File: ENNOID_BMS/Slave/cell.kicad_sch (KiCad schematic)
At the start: 6 parts, among them Q16 TSM2323

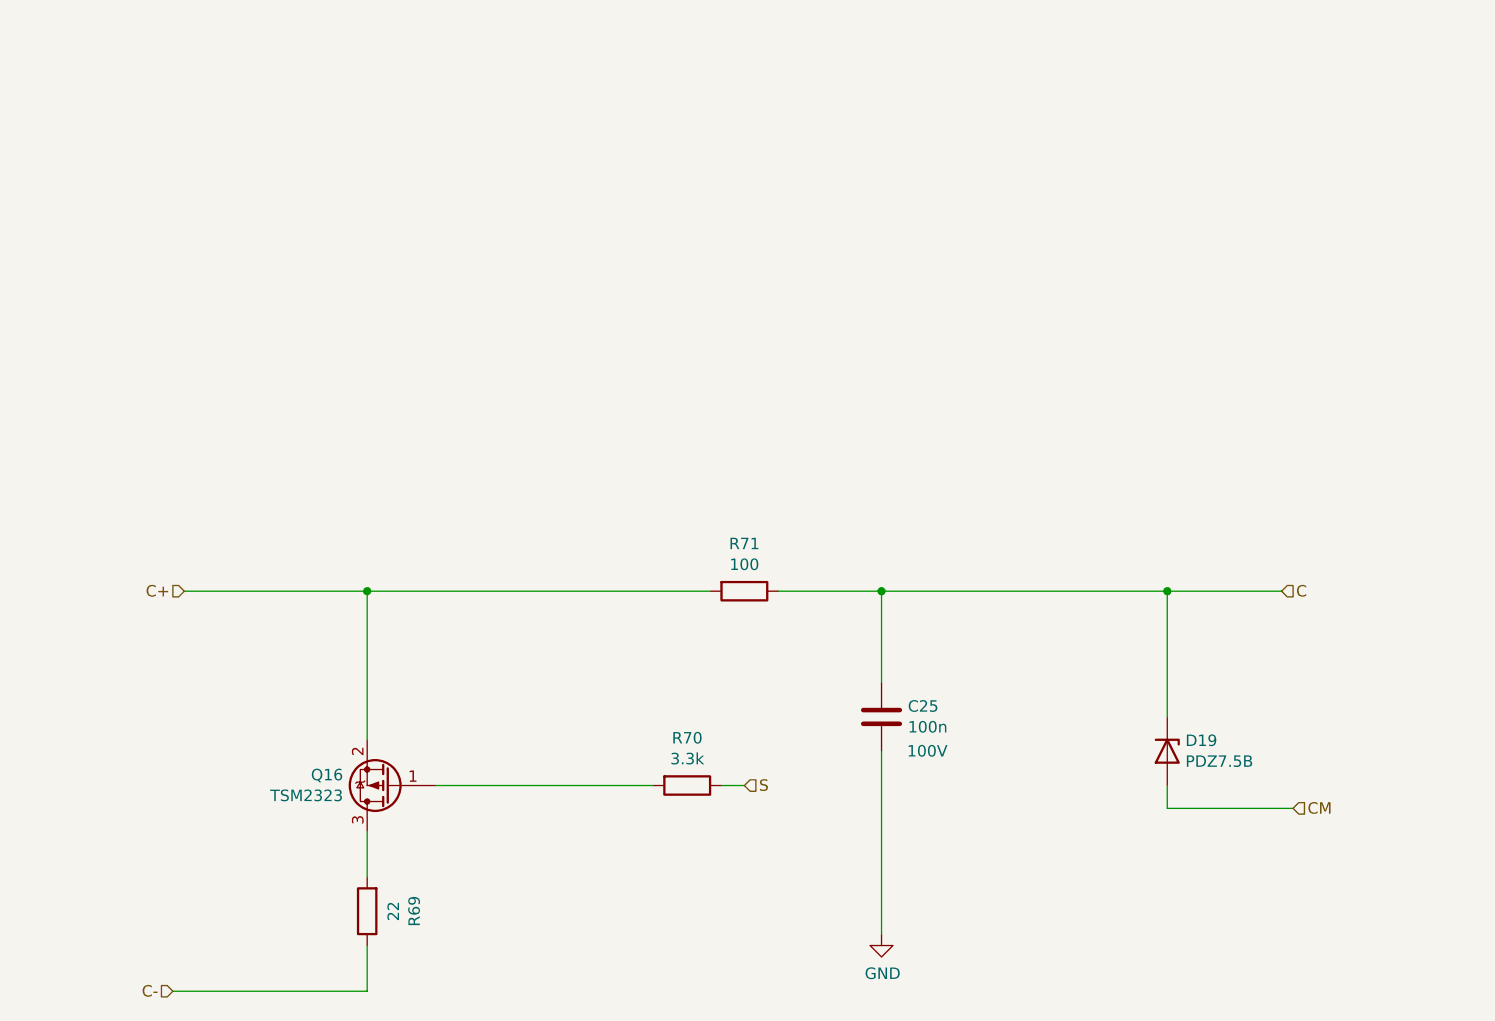
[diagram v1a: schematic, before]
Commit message: fused slave variant v1
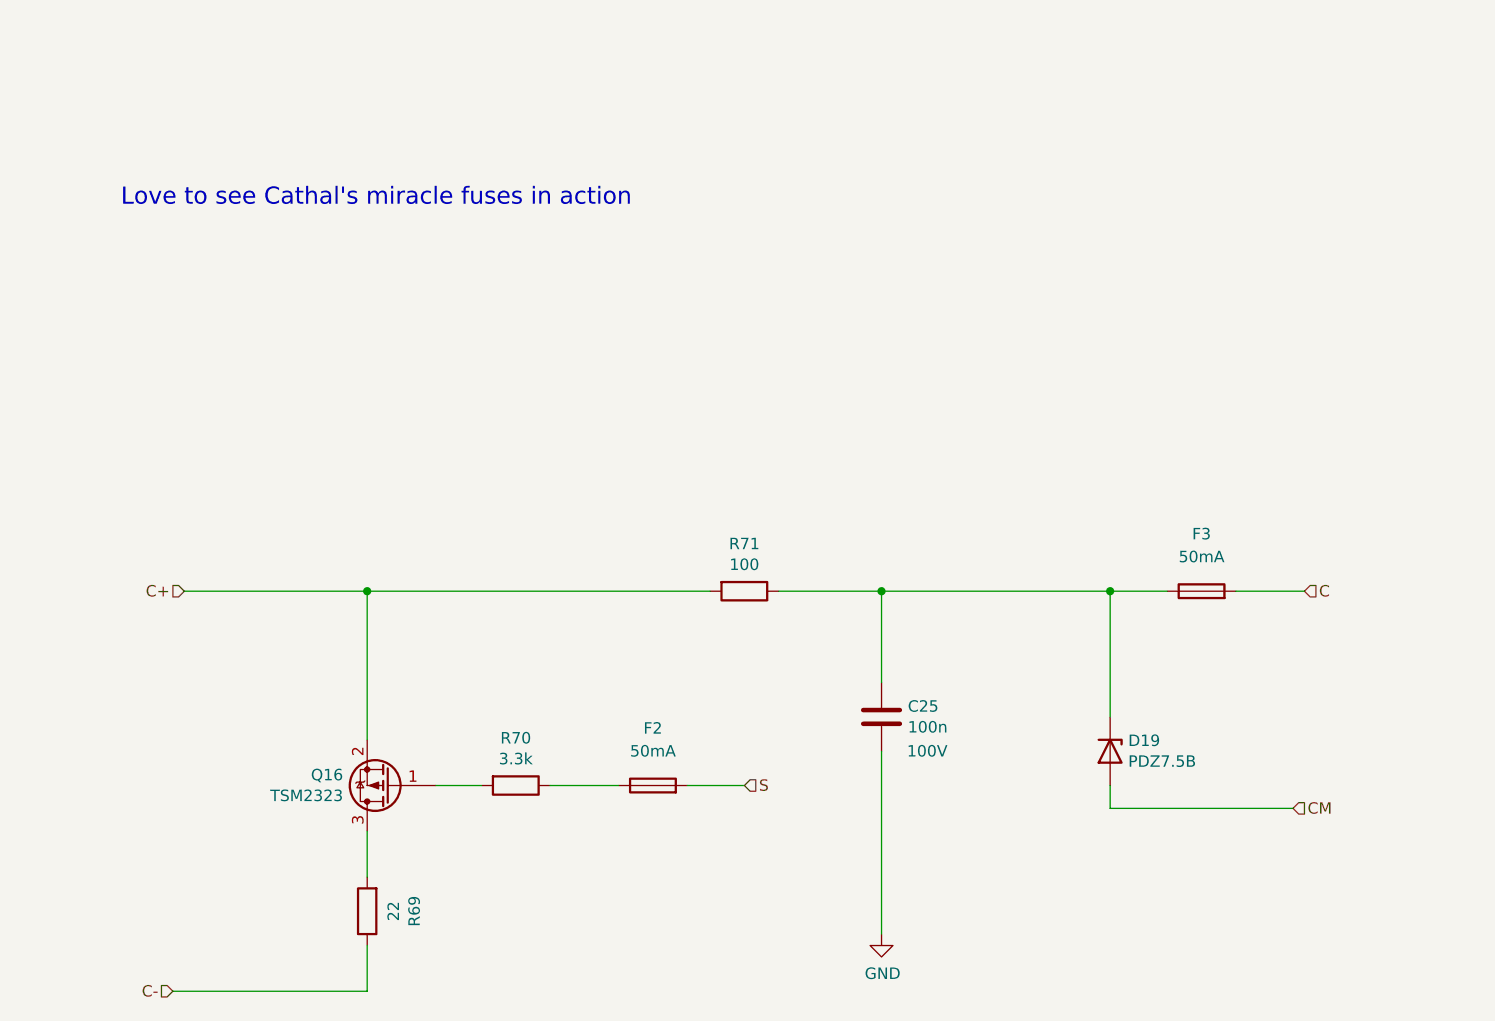
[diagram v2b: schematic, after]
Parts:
- added F2, F3: 50mA, Fuse:Fuse_0603_1608Metric, symbol Device:Fuse
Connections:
- net C: now also F3.2; no longer C25.2, D19.1 (K), R71.1
- net S: now also F2.2; no longer R70.1
- new net: C25.2, D19.1 (K), F3.1, R71.1
- new net: F2.1, R70.1
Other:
- note added: "Love to see Cathal's miracle fuses in action"
- moved on the sheet: D19, R70

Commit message: fuse boards
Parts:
- removed F2: 50mA, Fuse:Fuse_0603_1608Metric, symbol Device:Fuse
- Q16: Part Number TSM2323 -> TSM2323CX RFG
- R70: footprint Resistor_SMD:R_0603_1608Metric -> Resistor_SMD:R_0508_1220Metric; Part Number CRCW06033K30FKEA -> WK73R2ATTD3301F
- R71: Part Number CRCW0603100RFKEA -> RCS0603100RFKEA
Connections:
- net S: now also R70.1
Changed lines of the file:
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@@
 	(wire
 		(pts
-			(xy 106.68 104.14) (xy 114.3 104.14)
+			(xy 106.68 104.14) (xy 116.84 104.14)
 		)
 		(stroke
@@
 		(pts
 			(xy 66.04 82.55) (xy 86.36 82.55)
-		)
-		(stroke
-			(width 0)
-			(type default)
-		)
-	)
-	(wire
-		(pts
-			(xy 121.92 104.14) (xy 128.27 104.14)
 		)
 		(stroke
@@
 	(hierarchical_label "S"
 		(shape input)
-		(at 128.27 104.14 0)
+		(at 116.84 104.14 0)
 		(effects
 			(font
@@
 			)
 		)
-		(property "Datasheet" "https://www.vishay.com/docs/20043/crcwhpe3.pdf"
+		(property "Datasheet" "https://www.vishay.com/doc?20065"
 			(at 128.27 82.55 0)
 			(effects
@@
 			)
 		)
-		(property "Part Number" "CRCW0603100RFKEA"
+		(property "Part Number" "RCS0603100RFKEA"
 			(at 128.27 82.55 90)
 			(effects
@@
 			)
 		)
-		(property "Footprint" "Resistor_SMD:R_0603_1608Metric"
+		(property "Footprint" "Resistor_SMD:R_0508_1220Metric"
 			(at 102.87 102.362 90)
 			(effects
@@
 			)
 		)
-		(property "Datasheet" "https://www.vishay.com/docs/20035/dcrcwe3.pdf"
+		(property "Datasheet" "https://www.koaspeer.com/pdfs/WK73R.pdf"
 			(at 102.87 104.14 0)
 			(effects
@@
 			)
 		)
-		(property "Part Number" "CRCW06033K30FKEA"
+		(property "Part Number" "WK73R2ATTD3301F"
 			(at 102.87 104.14 90)
 			(effects
@@
 			)
 		)
-		(property "Part Number" "TSM2323"
+		(property "Part Number" "TSM2323CX RFG"
 			(at 88.9 104.14 0)
 			(effects
@@
 					(unit 1)
 				)
-			)
-		)
-	)
-	(symbol
-		(lib_id "Device:Fuse")
-		(at 118.11 104.14 90)
-		(unit 1)
-		(exclude_from_sim no)
-		(in_bom yes)
-		(on_board yes)
-		(dnp no)
-		(fields_autoplaced yes)
-		(property "Reference" "F2"
-			(at 118.11 97.79 90)
-			(effects
-				(font
-					(size 1.27 1.27)
-				)
-			)
-		)
-		(property "Value" "50mA"
-			(at 118.11 100.33 90)
-			(effects
-				(font
-					(size 1.27 1.27)
-				)
-			)
-		)
-		(property "Footprint" "Fuse:Fuse_0603_1608Metric"
-			(at 118.11 105.918 90)
-			(effects
-				(font
-					(size 1.27 1.27)
-				)
-				(hide yes)
-			)
-		)
-		(property "Datasheet" "https://www.farnell.com/datasheets/4426720.pdf"
-			(at 118.11 104.14 0)
-			(effects
-				(font
-					(size 1.27 1.27)
-				)
-				(hide yes)
-			)
-		)
-		(property "Description" "Fuse"
-			(at 118.11 104.14 0)
-			(effects
-				(font
-					(size 1.27 1.27)
-				)
-				(hide yes)
-			)
-		)
-		(property "Part Number" "F0603G0R05FNTR"
-			(at 118.11 104.14 90)
-			(effects
-				(font
-					(size 1.27 1.27)
-				)
-				(hide yes)
-			)
-		)
-		(pin "1"
-		)
-		(pin "2"
-		)
-		(instances
-			(project "LTC6812-15W"
-				(path "/2d3f1ad3-25f4-49ef-8b25-1989df14b0f9/00000000-0000-0000-0000-00005b4fcc47"
-					(reference "F33")
-					(unit 1)
-				)
-				(path "/2d3f1ad3-25f4-49ef-8b25-1989df14b0f9/00000000-0000-0000-0000-00005b4fd503"
-					(reference "F31")
-					(unit 1)
-				)
-				(path "/2d3f1ad3-25f4-49ef-8b25-1989df14b0f9/00000000-0000-0000-0000-00005b50012a"
-					(reference "F29")
-					(unit 1)
-				)
-				(path "/2d3f1ad3-25f4-49ef-8b25-1989df14b0f9/00000000-0000-0000-0000-00005b502fef"
-					(reference "F27")
-					(unit 1)
-				)
-				(path "/2d3f1ad3-25f4-49ef-8b25-1989df14b0f9/00000000-0000-0000-0000-00005b50355c"
-					(reference "F25")
-					(unit 1)
-				)
-				(path "/2d3f1ad3-25f4-49ef-8b25-1989df14b0f9/00000000-0000-0000-0000-00005b504105"
-					(reference "F23")
-					(unit 1)
-				)
-				(path "/2d3f1ad3-25f4-49ef-8b25-1989df14b0f9/00000000-0000-0000-0000-00005b504814"
-					(reference "F21")
-					(unit 1)
-				)
-				(path "/2d3f1ad3-25f4-49ef-8b25-1989df14b0f9/00000000-0000-0000-0000-00005b5050bc"
-					(reference "F16")
-					(unit 1)
-				)
-				(path "/2d3f1ad3-25f4-49ef-8b25-1989df14b0f9/00000000-0000-0000-0000-00005b50594b"
-					(reference "F14")
-					(unit 1)
-				)
-				(path "/2d3f1ad3-25f4-49ef-8b25-1989df14b0f9/00000000-0000-0000-0000-00005b506bb1"
-					(reference "F12")
-					(unit 1)
-				)
-				(path "/2d3f1ad3-25f4-49ef-8b25-1989df14b0f9/00000000-0000-0000-0000-00005b507536"
-					(reference "F10")
-					(unit 1)
-				)
-				(path "/2d3f1ad3-25f4-49ef-8b25-1989df14b0f9/00000000-0000-0000-0000-00005b50804f"
-					(reference "F8")
-					(unit 1)
-				)
-				(path "/2d3f1ad3-25f4-49ef-8b25-1989df14b0f9/00000000-0000-0000-0000-00005b508c6c"
-					(reference "F6")
-					(unit 1)
-				)
-				(path "/2d3f1ad3-25f4-49ef-8b25-1989df14b0f9/00000000-0000-0000-0000-00005b509a8b"
-					(reference "F4")
-					(unit 1)
-				)
-				(path "/2d3f1ad3-25f4-49ef-8b25-1989df14b0f9/00000000-0000-0000-0000-00005b50aaba"
-					(reference "F2")
-					(unit 1)
-				)
-			)
-			(project ""
-				(path "/952f467e-ad2b-47b9-b7a8-afd1294da234"
-					(reference "F1")
-					(unit 1)
-				)

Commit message: master and slave updated
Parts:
- F3: footprint Fuse:Fuse_0603_1608Metric -> Fuse:Fuse_1206_3216Metric; Part Number F0603G0R05FNTR -> 3413.0002.11
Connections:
- net C: now also C25.2, D19.1 (K)
- net at F3.1, R71.1: no longer C25.2, D19.1 (K)
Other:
- moved on the sheet: C25, D19, F3, R71
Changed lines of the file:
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@@
 	(text "Love to see Cathal's miracle fuses in action"
 		(exclude_from_sim no)
-		(at 87.376 38.862 0)
+		(at 88.9 21.082 0)
 		(effects
 			(font
@@
 			)
 		)
-	)
-	(junction
-		(at 168.91 82.55)
-		(diameter 0)
-		(color 0 0 0 0)
 	)
 	(junction
@@
 	)
 	(junction
-		(at 143.51 82.55)
+		(at 158.75 82.55)
 		(diameter 0)
 		(color 0 0 0 0)
 	)
-	(wire
-		(pts
-			(xy 168.91 96.52) (xy 168.91 82.55)
-		)
-		(stroke
-			(width 0)
-			(type default)
-		)
-	)
-	(wire
-		(pts
-			(xy 143.51 82.55) (xy 143.51 92.71)
+	(junction
+		(at 184.15 82.55)
+		(diameter 0)
+		(color 0 0 0 0)
+	)
+	(wire
+		(pts
+			(xy 148.59 82.55) (xy 158.75 82.55)
+		)
+		(stroke
+			(width 0)
+			(type default)
+		)
+	)
+	(wire
+		(pts
+			(xy 184.15 96.52) (xy 184.15 82.55)
+		)
+		(stroke
+			(width 0)
+			(type default)
+		)
+	)
+	(wire
+		(pts
+			(xy 158.75 82.55) (xy 158.75 92.71)
 		)
 		(stroke
@@
 	(wire
 		(pts
-			(xy 168.91 106.68) (xy 189.23 106.68)
-		)
-		(stroke
-			(width 0)
-			(type default)
-		)
-	)
-	(wire
-		(pts
-			(xy 86.36 82.55) (xy 124.46 82.55)
+			(xy 184.15 106.68) (xy 204.47 106.68)
+		)
+		(stroke
+			(width 0)
+			(type default)
+		)
+	)
+	(wire
+		(pts
+			(xy 184.15 82.55) (xy 205.74 82.55)
+		)
+		(stroke
+			(width 0)
+			(type default)
+		)
+	)
+	(wire
+		(pts
+			(xy 86.36 82.55) (xy 110.49 82.55)
 		)
 		(stroke
@@
 	(wire
 		(pts
-			(xy 143.51 100.33) (xy 143.51 120.65)
+			(xy 118.11 82.55) (xy 140.97 82.55)
+		)
+		(stroke
+			(width 0)
+			(type default)
+		)
+	)
+	(wire
+		(pts
+			(xy 158.75 100.33) (xy 158.75 120.65)
 		)
 		(stroke
@@
 	(wire
 		(pts
-			(xy 168.91 104.14) (xy 168.91 106.68)
+			(xy 184.15 104.14) (xy 184.15 106.68)
 		)
 		(stroke
@@
 	(wire
 		(pts
-			(xy 143.51 82.55) (xy 168.91 82.55)
-		)
-		(stroke
-			(width 0)
-			(type default)
-		)
-	)
-	(wire
-		(pts
-			(xy 132.08 82.55) (xy 143.51 82.55)
-		)
-		(stroke
-			(width 0)
-			(type default)
-		)
-	)
-	(wire
-		(pts
-			(xy 182.88 82.55) (xy 190.5 82.55)
+			(xy 158.75 82.55) (xy 184.15 82.55)
 		)
 		(stroke
@@
 		(pts
 			(xy 93.98 104.14) (xy 99.06 104.14)
-		)
-		(stroke
-			(width 0)
-			(type default)
-		)
-	)
-	(wire
-		(pts
-			(xy 168.91 82.55) (xy 175.26 82.55)
 		)
 		(stroke
@@
 	(hierarchical_label "C"
 		(shape input)
-		(at 190.5 82.55 0)
+		(at 205.74 82.55 0)
 		(effects
 			(font
@@
 	(hierarchical_label "CM"
 		(shape input)
-		(at 189.23 106.68 0)
+		(at 204.47 106.68 0)
 		(effects
 			(font
@@
 	(symbol
 		(lib_id "Device:R")
-		(at 128.27 82.55 270)
+		(at 114.3 82.55 270)
 		(unit 1)
 		(exclude_from_sim no)
@@
 		(dnp no)
 		(property "Reference" "R71"
-			(at 128.27 77.2922 90)
+			(at 114.3 77.2922 90)
 			(effects
 				(font
@@
 		)
 		(property "Value" "100"
-			(at 128.27 79.6036 90)
+			(at 114.3 79.6036 90)
 			(effects
 				(font
@@
 		)
 		(property "Footprint" "Resistor_SMD:R_0603_1608Metric"
-			(at 128.27 80.772 90)
+			(at 114.3 80.772 90)
 			(effects
 				(font
@@
 		)
 		(property "Datasheet" "https://www.vishay.com/doc?20065"
-			(at 128.27 82.55 0)
+			(at 114.3 82.55 0)
 			(effects
 				(font
@@
 		)
 		(property "Description" ""
-			(at 128.27 82.55 0)
+			(at 114.3 82.55 0)
 			(effects
 				(font
@@
 		)
 		(property "Part Number" "RCS0603100RFKEA"
-			(at 128.27 82.55 90)
+			(at 114.3 82.55 90)
 			(effects
 				(font
@@
 	(symbol
 		(lib_id "Device:C")
-		(at 143.51 96.52 180)
+		(at 158.75 96.52 180)
 		(unit 1)
 		(exclude_from_sim no)
@@
 		(dnp no)
 		(property "Reference" "C25"
-			(at 146.431 95.3516 0)
+			(at 161.671 95.3516 0)
 			(effects
 				(font
@@
 		)
 		(property "Value" "100n"
-			(at 146.431 97.663 0)
+			(at 161.671 97.663 0)
 			(effects
 				(font
@@
 		)
 		(property "Footprint" "Capacitor_SMD:C_0603_1608Metric"
-			(at 142.5448 92.71 0)
+			(at 157.7848 92.71 0)
 			(effects
 				(font
@@
 		)
 		(property "Datasheet" "https://pim.murata.com/asset/pim4/ceramicCapacitorSMD/GRM188R72A104KA35-01A-EN_PDF_CERAMICCAPACITORSMD"
-			(at 143.51 96.52 0)
+			(at 158.75 96.52 0)
 			(effects
 				(font
@@
 		)
 		(property "Description" ""
-			(at 143.51 96.52 0)
+			(at 158.75 96.52 0)
 			(effects
 				(font
@@
 		)
 		(property "Voltage" "100V"
-			(at 148.59 100.33 0)
+			(at 163.83 100.33 0)
 			(effects
 				(font
@@
 		)
 		(property "Part Number" "GRM188R72A104KA35D"
-			(at 143.51 96.52 0)
+			(at 158.75 96.52 0)
 			(effects
 				(font
@@
 	(symbol
 		(lib_id "Device:D_Zener")
-		(at 168.91 100.33 270)
+		(at 184.15 100.33 270)
 		(unit 1)
 		(exclude_from_sim no)
@@
 		(dnp no)
 		(property "Reference" "D19"
-			(at 170.9166 99.1616 90)
+			(at 186.1566 99.1616 90)
 			(effects
 				(font
@@
 		)
 		(property "Value" "PDZ7.5B"
-			(at 170.9166 101.473 90)
+			(at 186.1566 101.473 90)
 			(effects
 				(font
@@
 		)
 		(property "Footprint" "Diode_SMD:D_SOD-323"
-			(at 168.91 100.33 0)
+			(at 184.15 100.33 0)
 			(effects
 				(font
@@
 		)
 		(property "Datasheet" "https://assets.nexperia.com/documents/data-sheet/PDZ-B_SER.pdf"
-			(at 168.91 100.33 0)
+			(at 184.15 100.33 0)
 			(effects
 				(font
@@
 		)
 		(property "Description" ""
-			(at 168.91 100.33 0)
+			(at 184.15 100.33 0)
 			(effects
 				(font
@@
 		)
 		(property "Part Number" "PDZ7.5B"
-			(at 168.91 100.33 90)
+			(at 184.15 100.33 90)
 			(effects
 				(font
@@
 	(symbol
 		(lib_id "power:GND")
-		(at 143.51 120.65 0)
+		(at 158.75 120.65 0)
 		(unit 1)
 		(exclude_from_sim no)
@@
 		(dnp no)
 		(property "Reference" "#PWR036"
-			(at 143.51 127 0)
+			(at 158.75 127 0)
 			(effects
 				(font
@@
 		)
 		(property "Value" "GND"
-			(at 143.637 125.0442 0)
+			(at 158.877 125.0442 0)
 			(effects
 				(font
@@
 		)
 		(property "Footprint" ""
-			(at 143.51 120.65 0)
+			(at 158.75 120.65 0)
 			(effects
 				(font
@@
 		)
 		(property "Datasheet" ""
-			(at 143.51 120.65 0)
+			(at 158.75 120.65 0)
 			(effects
 				(font
@@
 		)
 		(property "Description" ""
-			(at 143.51 120.65 0)
+			(at 158.75 120.65 0)
 			(effects
 				(font
@@
 	(symbol
 		(lib_id "Device:Fuse")
-		(at 179.07 82.55 90)
+		(at 144.78 82.55 90)
 		(unit 1)
 		(exclude_from_sim no)
@@
 		(fields_autoplaced yes)
 		(property "Reference" "F3"
-			(at 179.07 76.2 90)
+			(at 144.78 76.2 90)
 			(effects
 				(font
@@
 		)
 		(property "Value" "50mA"
-			(at 179.07 78.74 90)
-			(effects
-				(font
-					(size 1.27 1.27)
-				)
-			)
-		)
-		(property "Footprint" "Fuse:Fuse_0603_1608Metric"
-			(at 179.07 84.328 90)
-			(effects
-				(font
-					(size 1.27 1.27)
-				)
-				(hide yes)
-			)
-		)
-		(property "Datasheet" "https://www.farnell.com/datasheets/4426720.pdf"
-			(at 179.07 82.55 0)
+			(at 144.78 78.74 90)
+			(effects
+				(font
+					(size 1.27 1.27)
+				)
+			)
+		)
+		(property "Footprint" "Fuse:Fuse_1206_3216Metric"
+			(at 144.78 84.328 90)
+			(effects
+				(font
+					(size 1.27 1.27)
+				)
+				(hide yes)
+			)
+		)
+		(property "Datasheet" "https://www.mouser.ie/datasheet/3/386/1/typ_USFF_1206.pdf"
+			(at 144.78 82.55 0)
 			(effects
 				(font
@@
 		)
 		(property "Description" "Fuse"
-			(at 179.07 82.55 0)
-			(effects
-				(font
-					(size 1.27 1.27)
-				)
-				(hide yes)
-			)
-		)
-		(property "Part Number" "F0603G0R05FNTR"
-			(at 179.07 82.55 90)
-			(effects
-				(font
+			(at 144.78 82.55 0)
+			(effects
+				(font
+					(size 1.27 1.27)
+				)
+				(hide yes)
+			)
+		)
+		(property "Part Number" "3413.0002.11"
+			(at 144.78 82.55 90)
+			(effects
+				(font

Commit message: new cells and updated slave
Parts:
- R71: footprint Resistor_SMD:R_0603_1608Metric -> Resistor_SMD:R_0805_2012Metric; Part Number RCS0603100RFKEA -> CRCW0805100RFKEAHP
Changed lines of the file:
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@@
 			)
 		)
-		(property "Footprint" "Resistor_SMD:R_0603_1608Metric"
+		(property "Footprint" "Resistor_SMD:R_0805_2012Metric"
 			(at 114.3 80.772 90)
 			(effects
@@
 			)
 		)
-		(property "Datasheet" "https://www.vishay.com/doc?20065"
+		(property "Datasheet" "https://www.vishay.com/docs/20043/crcwhpe3.pdf"
 			(at 114.3 82.55 0)
 			(effects
@@
 			)
 		)
-		(property "Part Number" "RCS0603100RFKEA"
+		(property "Part Number" "CRCW0805100RFKEAHP"
 			(at 114.3 82.55 90)
 			(effects
